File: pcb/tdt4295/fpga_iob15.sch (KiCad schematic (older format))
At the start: 8 parts, among them U102 XC7A100T-FTG256-tdt4295

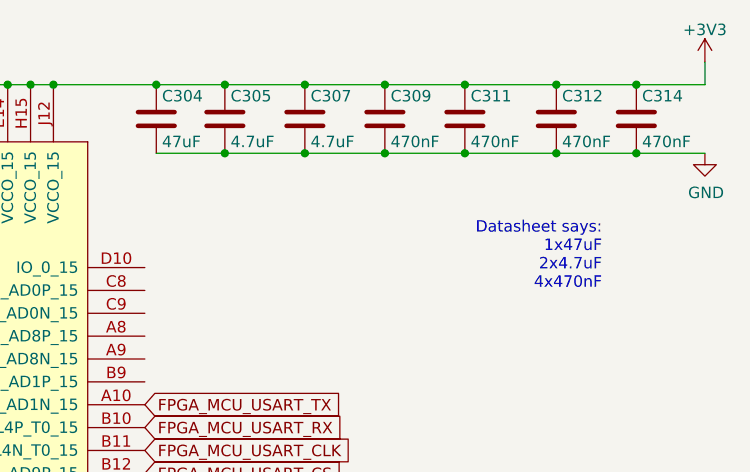
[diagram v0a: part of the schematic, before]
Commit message: associate (most) symbols with footprints
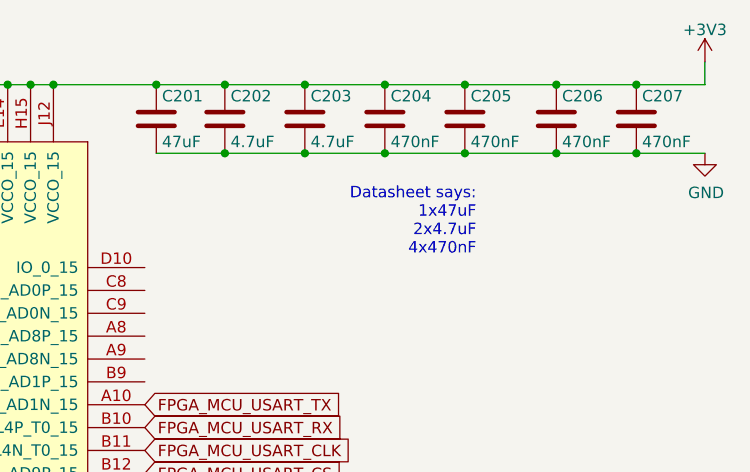
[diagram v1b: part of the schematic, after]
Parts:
- C201: renamed from C304; footprint (none) -> Capacitor_SMD:C_1210_3225Metric_Pad1.33x2.70mm_HandSolder; Component name (none) -> GRM32ER71A476ME15L
- C204: renamed from C309; footprint (none) -> Capacitor_SMD:C_0603_1608Metric_Pad1.08x0.95mm_HandSolder; Component name (none) -> GRM188R71C474KA88D
- C205: renamed from C311; footprint (none) -> Capacitor_SMD:C_0603_1608Metric_Pad1.08x0.95mm_HandSolder; Component name (none) -> GRM188R71C474KA88D
- C206: renamed from C312; footprint (none) -> Capacitor_SMD:C_0603_1608Metric_Pad1.08x0.95mm_HandSolder; Component name (none) -> GRM188R71C474KA88D
- C207: renamed from C314; footprint (none) -> Capacitor_SMD:C_0603_1608Metric_Pad1.08x0.95mm_HandSolder; Component name (none) -> GRM188R71C474KA88D
- renumbered C305 to C202, C307 to C203
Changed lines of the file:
@@
 Connection ~ 1950 900
 $Comp
-L power:GND #PWR0301
+L power:GND #PWR0202
 U 1 1 614E24A1
 P 4800 1200
-F 0 "#PWR0301" H 4800 950 50  0001 C CNN
+F 0 "#PWR0202" H 4800 950 50  0001 C CNN
 F 1 "GND" H 4805 1027 50  0000 C CNN
 F 2 "" H 4800 1200 50  0001 C CNN
@@
 P 2400 1050
 AR Path="/61459CB7/615F1C9B" Ref="C?"  Part="1"
-AR Path="/614933B1/615F1C9B" Ref="C304"  Part="1"
-F 0 "C304" H 2425 1150 50  0000 L CNN
+AR Path="/614933B1/615F1C9B" Ref="C201"  Part="1"
+F 0 "C201" H 2425 1150 50  0000 L CNN
 F 1 "47uF" H 2425 950 50  0000 L CNN
-F 2 "" H 2438 900 50  0001 C CNN
-F 3 "~" H 2400 1050 50  0001 C CNN
+F 2 "Capacitor_SMD:C_1210_3225Metric_Pad1.33x2.70mm_HandSolder" H 2438 900 50  0001 C CNN
+F 3 "https://www.farnell.com/datasheets/2047839.pdf" H 2400 1050 50  0001 C CNN
+F 4 "GRM32ER71A476ME15L" H 2400 1050 50  0001 C CNN "Component name"
 	1    2400 1050
 	1    0    0    -1
@@
 P 2700 1050
 AR Path="/61459CB7/615F1CA1" Ref="C?"  Part="1"
-AR Path="/614933B1/615F1CA1" Ref="C305"  Part="1"
-F 0 "C305" H 2725 1150 50  0000 L CNN
+AR Path="/614933B1/615F1CA1" Ref="C202"  Part="1"
+F 0 "C202" H 2725 1150 50  0000 L CNN
 F 1 "4.7uF" H 2725 950 50  0000 L CNN
 F 2 "Capacitor_SMD:C_0805_2012Metric_Pad1.18x1.45mm_HandSolder" H 2738 900 50  0001 C CNN
@@
 P 3050 1050
 AR Path="/61459CB7/615F1CA7" Ref="C?"  Part="1"
-AR Path="/614933B1/615F1CA7" Ref="C307"  Part="1"
-F 0 "C307" H 3075 1150 50  0000 L CNN
+AR Path="/614933B1/615F1CA7" Ref="C203"  Part="1"
+F 0 "C203" H 3075 1150 50  0000 L CNN
 F 1 "4.7uF" H 3075 950 50  0000 L CNN
 F 2 "Capacitor_SMD:C_0805_2012Metric_Pad1.18x1.45mm_HandSolder" H 3088 900 50  0001 C CNN
@@
 P 3400 1050
 AR Path="/61459CB7/615F1CAD" Ref="C?"  Part="1"
-AR Path="/614933B1/615F1CAD" Ref="C309"  Part="1"
-F 0 "C309" H 3425 1150 50  0000 L CNN
+AR Path="/614933B1/615F1CAD" Ref="C204"  Part="1"
+F 0 "C204" H 3425 1150 50  0000 L CNN
 F 1 "470nF" H 3425 950 50  0000 L CNN
-F 2 "" H 3438 900 50  0001 C CNN
-F 3 "~" H 3400 1050 50  0001 C CNN
+F 2 "Capacitor_SMD:C_0603_1608Metric_Pad1.08x0.95mm_HandSolder" H 3438 900 50  0001 C CNN
+F 3 "https://www.farnell.com/datasheets/2048812.pdf" H 3400 1050 50  0001 C CNN
+F 4 "GRM188R71C474KA88D" H 3400 1050 50  0001 C CNN "Component name"
 	1    3400 1050
 	1    0    0    -1
@@
 P 3750 1050
 AR Path="/61459CB7/615F1CB3" Ref="C?"  Part="1"
-AR Path="/614933B1/615F1CB3" Ref="C311"  Part="1"
-F 0 "C311" H 3775 1150 50  0000 L CNN
+AR Path="/614933B1/615F1CB3" Ref="C205"  Part="1"
+F 0 "C205" H 3775 1150 50  0000 L CNN
 F 1 "470nF" H 3775 950 50  0000 L CNN
-F 2 "" H 3788 900 50  0001 C CNN
-F 3 "~" H 3750 1050 50  0001 C CNN
+F 2 "Capacitor_SMD:C_0603_1608Metric_Pad1.08x0.95mm_HandSolder" H 3788 900 50  0001 C CNN
+F 3 "https://www.farnell.com/datasheets/2048812.pdf" H 3750 1050 50  0001 C CNN
+F 4 "GRM188R71C474KA88D" H 3750 1050 50  0001 C CNN "Component name"
 	1    3750 1050
 	1    0    0    -1
@@
 P 4150 1050
 AR Path="/61459CB7/615F1CB9" Ref="C?"  Part="1"
-AR Path="/614933B1/615F1CB9" Ref="C312"  Part="1"
-F 0 "C312" H 4175 1150 50  0000 L CNN
+AR Path="/614933B1/615F1CB9" Ref="C206"  Part="1"
+F 0 "C206" H 4175 1150 50  0000 L CNN
 F 1 "470nF" H 4175 950 50  0000 L CNN
-F 2 "" H 4188 900 50  0001 C CNN
-F 3 "~" H 4150 1050 50  0001 C CNN
+F 2 "Capacitor_SMD:C_0603_1608Metric_Pad1.08x0.95mm_HandSolder" H 4188 900 50  0001 C CNN
+F 3 "https://www.farnell.com/datasheets/2048812.pdf" H 4150 1050 50  0001 C CNN
+F 4 "GRM188R71C474KA88D" H 4150 1050 50  0001 C CNN "Component name"
 	1    4150 1050
 	1    0    0    -1
@@
 P 4500 1050
 AR Path="/61459CB7/615F1CBF" Ref="C?"  Part="1"
-AR Path="/614933B1/615F1CBF" Ref="C314"  Part="1"
-F 0 "C314" H 4525 1150 50  0000 L CNN
+AR Path="/614933B1/615F1CBF" Ref="C207"  Part="1"
+F 0 "C207" H 4525 1150 50  0000 L CNN
 F 1 "470nF" H 4525 950 50  0000 L CNN
-F 2 "" H 4538 900 50  0001 C CNN
-F 3 "~" H 4500 1050 50  0001 C CNN
+F 2 "Capacitor_SMD:C_0603_1608Metric_Pad1.08x0.95mm_HandSolder" H 4538 900 50  0001 C CNN
+F 3 "https://www.farnell.com/datasheets/2048812.pdf" H 4500 1050 50  0001 C CNN
+F 4 "GRM188R71C474KA88D" H 4500 1050 50  0001 C CNN "Component name"
 	1    4500 1050
 	1    0    0    -1
 $EndComp
-Text Notes 4350 1800 2    50   ~ 0
+Text Notes 3800 1650 2    50   ~ 0
 Datasheet says:\n1x47uF\n2x4.7uF\n4x470nF
 Text GLabel 2350 2300 2    50   Input ~ 0
@@
 	4800 900  4800 800
 $Comp
-L power:+3V3 #PWR?
+L power:+3V3 #PWR0201
 U 1 1 61732788
 P 4800 800
-F 0 "#PWR?" H 4800 650 50  0001 C CNN
+F 0 "#PWR0201" H 4800 650 50  0001 C CNN
 F 1 "+3V3" H 4800 940 50  0000 C CNN
 F 2 "" H 4800 800 50  0001 C CNN

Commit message: add final footprints, tweak VGA output
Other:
- note removed: "Datasheet says:\n1x47uF\n2x4.7uF\n4x470nF"
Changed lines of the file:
@@
 	1    0    0    -1
 $EndComp
-Text Notes 3800 1650 2    50   ~ 0
-Datasheet says:\n1x47uF\n2x4.7uF\n4x470nF
 Text GLabel 2350 2300 2    50   Input ~ 0
 FPGA_MCU_USART_TX

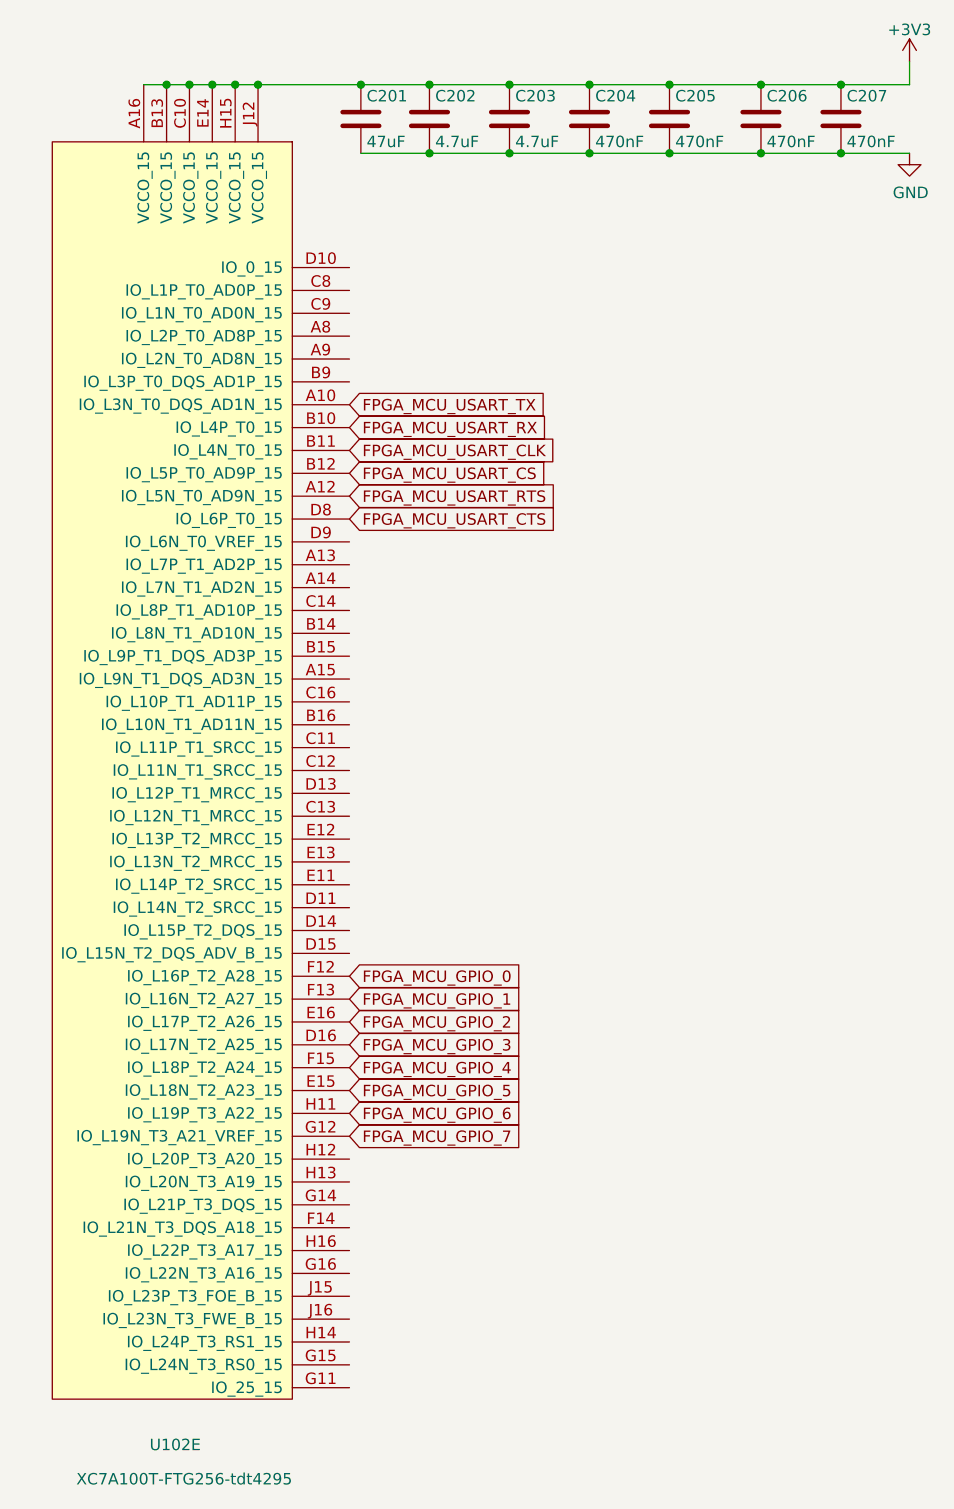
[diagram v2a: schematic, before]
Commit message: Add some no connection symbols
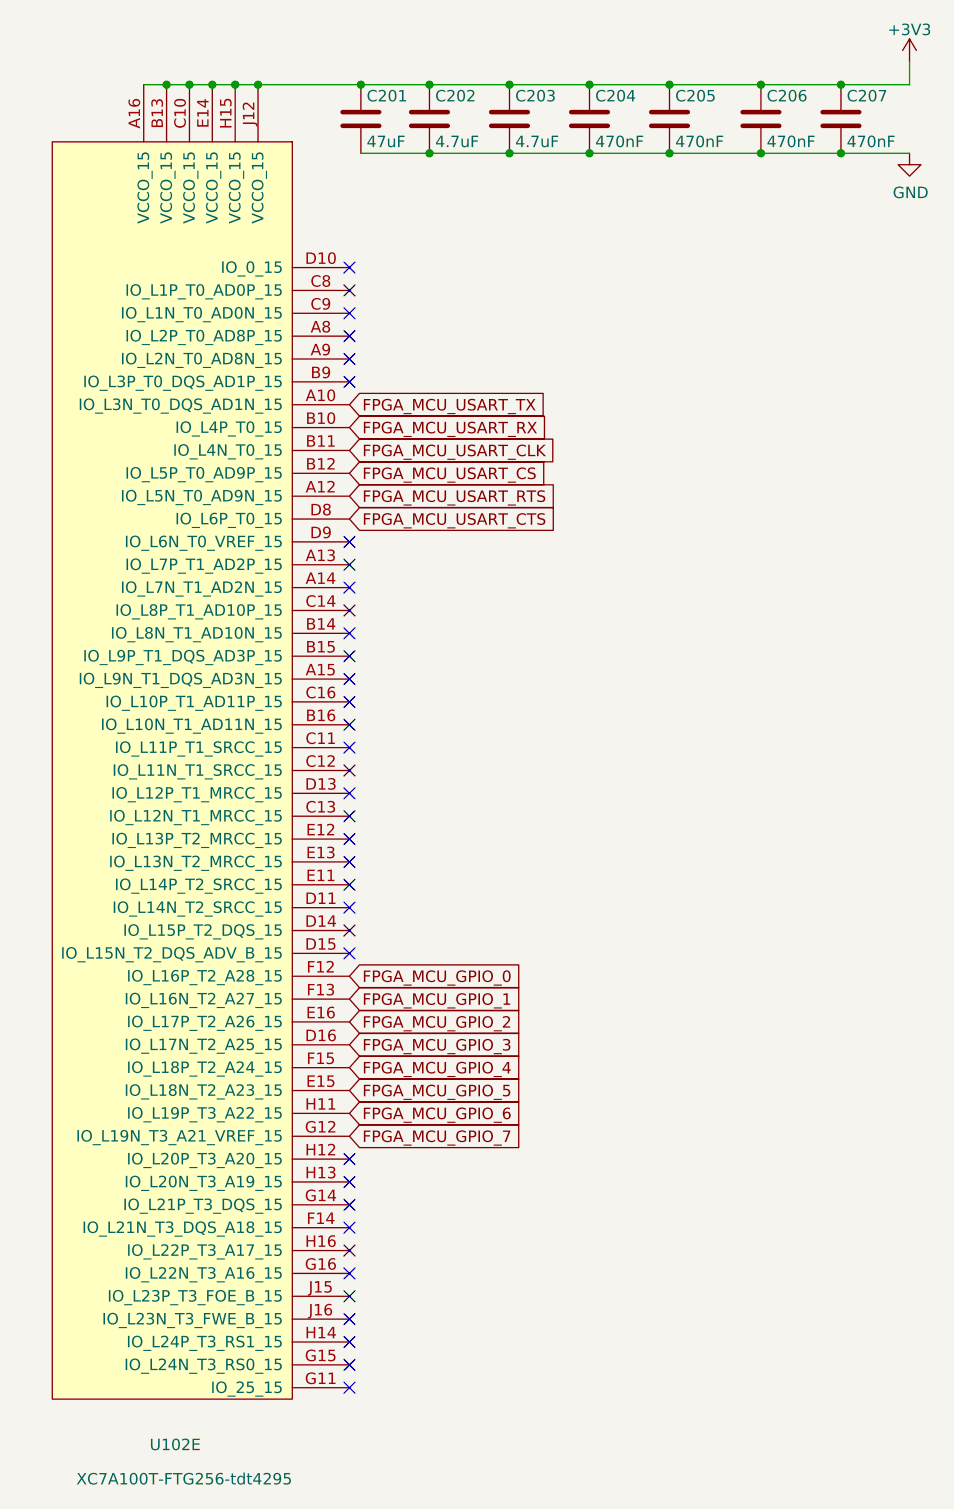
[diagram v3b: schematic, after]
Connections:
- no-connect marks 0 -> 36
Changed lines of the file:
@@
 Wire Wire Line
 	4500 1200 4800 1200
+NoConn ~ 2350 1700
+NoConn ~ 2350 1800
+NoConn ~ 2350 1900
+NoConn ~ 2350 2000
+NoConn ~ 2350 2100
+NoConn ~ 2350 2200
+NoConn ~ 2350 2900
+NoConn ~ 2350 3000
+NoConn ~ 2350 3100
+NoConn ~ 2350 3200
+NoConn ~ 2350 3300
+NoConn ~ 2350 3400
+NoConn ~ 2350 3500
+NoConn ~ 2350 3600
+NoConn ~ 2350 3700
+NoConn ~ 2350 3800
+NoConn ~ 2350 3900
+NoConn ~ 2350 4000
+NoConn ~ 2350 4100
+NoConn ~ 2350 4200
+NoConn ~ 2350 4300
+NoConn ~ 2350 4400
+NoConn ~ 2350 4500
+NoConn ~ 2350 4600
+NoConn ~ 2350 4700
+NoConn ~ 2350 5600
+NoConn ~ 2350 5700
+NoConn ~ 2350 5800
+NoConn ~ 2350 5900
+NoConn ~ 2350 6000
+NoConn ~ 2350 6100
+NoConn ~ 2350 6200
+NoConn ~ 2350 6300
+NoConn ~ 2350 6400
+NoConn ~ 2350 6500
+NoConn ~ 2350 6600
 $EndSCHEMATC

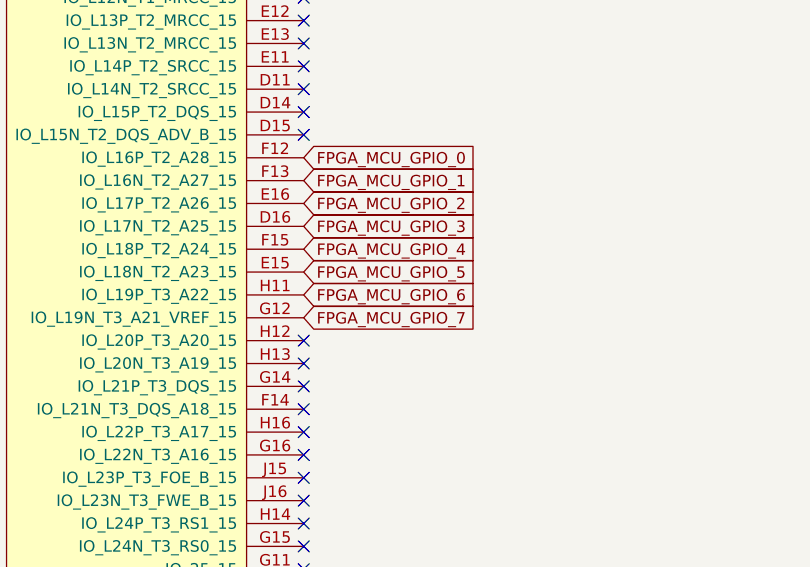
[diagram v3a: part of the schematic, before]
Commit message: cut 4 gpio connections between fpga/mcu
more flexible to keep more gpio pins on header
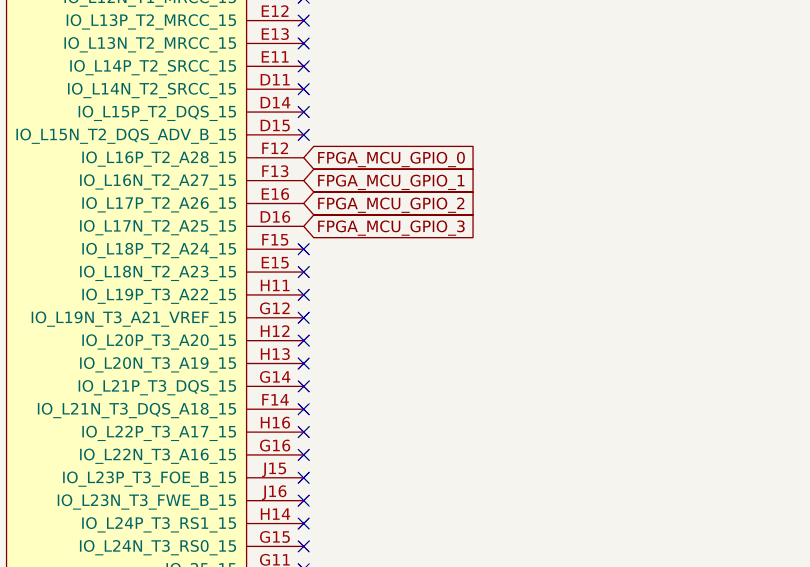
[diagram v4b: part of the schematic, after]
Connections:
- net FPGA_MCU_GPIO_4: no longer names the net of U102.F15 (IO_L18P_T2_A24_15)
- net FPGA_MCU_GPIO_5: no longer names the net of U102.E15 (IO_L18N_T2_A23_15)
- net FPGA_MCU_GPIO_6: no longer names the net of U102.H11 (IO_L19P_T3_A22_15)
- net FPGA_MCU_GPIO_7: no longer names the net of U102.G12 (IO_L19N_T3_A21_VREF_15)
- no-connect marks 36 -> 40
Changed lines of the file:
@@
 $Descr A4 11693 8268
 encoding utf-8
-Sheet 2 4
+Sheet 4 6
 Title ""
 Date ""
@@
 AR Path="/61459CB7/615F1C9B" Ref="C?"  Part="1"
 AR Path="/614933B1/615F1C9B" Ref="C201"  Part="1"
+AR Path="/617F72AC/614933B1/615F1C9B" Ref="C201"  Part="1"
 F 0 "C201" H 2425 1150 50  0000 L CNN
 F 1 "47uF" H 2425 950 50  0000 L CNN
@@
 AR Path="/61459CB7/615F1CA1" Ref="C?"  Part="1"
 AR Path="/614933B1/615F1CA1" Ref="C202"  Part="1"
+AR Path="/617F72AC/614933B1/615F1CA1" Ref="C202"  Part="1"
 F 0 "C202" H 2725 1150 50  0000 L CNN
 F 1 "4.7uF" H 2725 950 50  0000 L CNN
@@
 AR Path="/61459CB7/615F1CA7" Ref="C?"  Part="1"
 AR Path="/614933B1/615F1CA7" Ref="C203"  Part="1"
+AR Path="/617F72AC/614933B1/615F1CA7" Ref="C203"  Part="1"
 F 0 "C203" H 3075 1150 50  0000 L CNN
 F 1 "4.7uF" H 3075 950 50  0000 L CNN
@@
 AR Path="/61459CB7/615F1CAD" Ref="C?"  Part="1"
 AR Path="/614933B1/615F1CAD" Ref="C204"  Part="1"
+AR Path="/617F72AC/614933B1/615F1CAD" Ref="C204"  Part="1"
 F 0 "C204" H 3425 1150 50  0000 L CNN
 F 1 "470nF" H 3425 950 50  0000 L CNN
@@
 AR Path="/61459CB7/615F1CB3" Ref="C?"  Part="1"
 AR Path="/614933B1/615F1CB3" Ref="C205"  Part="1"
+AR Path="/617F72AC/614933B1/615F1CB3" Ref="C205"  Part="1"
 F 0 "C205" H 3775 1150 50  0000 L CNN
 F 1 "470nF" H 3775 950 50  0000 L CNN
@@
 AR Path="/61459CB7/615F1CB9" Ref="C?"  Part="1"
 AR Path="/614933B1/615F1CB9" Ref="C206"  Part="1"
+AR Path="/617F72AC/614933B1/615F1CB9" Ref="C206"  Part="1"
 F 0 "C206" H 4175 1150 50  0000 L CNN
 F 1 "470nF" H 4175 950 50  0000 L CNN
@@
 AR Path="/61459CB7/615F1CBF" Ref="C?"  Part="1"
 AR Path="/614933B1/615F1CBF" Ref="C207"  Part="1"
+AR Path="/617F72AC/614933B1/615F1CBF" Ref="C207"  Part="1"
 F 0 "C207" H 4525 1150 50  0000 L CNN
 F 1 "470nF" H 4525 950 50  0000 L CNN
@@
 Text GLabel 2350 5100 2    50   Input ~ 0
 FPGA_MCU_GPIO_3
-Text GLabel 2350 5200 2    50   Input ~ 0
-FPGA_MCU_GPIO_4
-Text GLabel 2350 5300 2    50   Input ~ 0
-FPGA_MCU_GPIO_5
-Text GLabel 2350 5400 2    50   Input ~ 0
-FPGA_MCU_GPIO_6
-Text GLabel 2350 5500 2    50   Input ~ 0
-FPGA_MCU_GPIO_7
 Wire Wire Line
 	4800 900  4800 800
@@
 NoConn ~ 2350 6500
 NoConn ~ 2350 6600
+NoConn ~ 2350 5200
+NoConn ~ 2350 5300
+NoConn ~ 2350 5400
+NoConn ~ 2350 5500
 $EndSCHEMATC
